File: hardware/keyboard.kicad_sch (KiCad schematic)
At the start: 10 parts, among them SW11 SW_Push, SW12 SW_Push, SW13 SW_Push, SW14 SW_Push, SW15 SW_Push, SW16 SW_Push, SW17 SW_Push, SW18 SW_Push, SW19 SW_Push

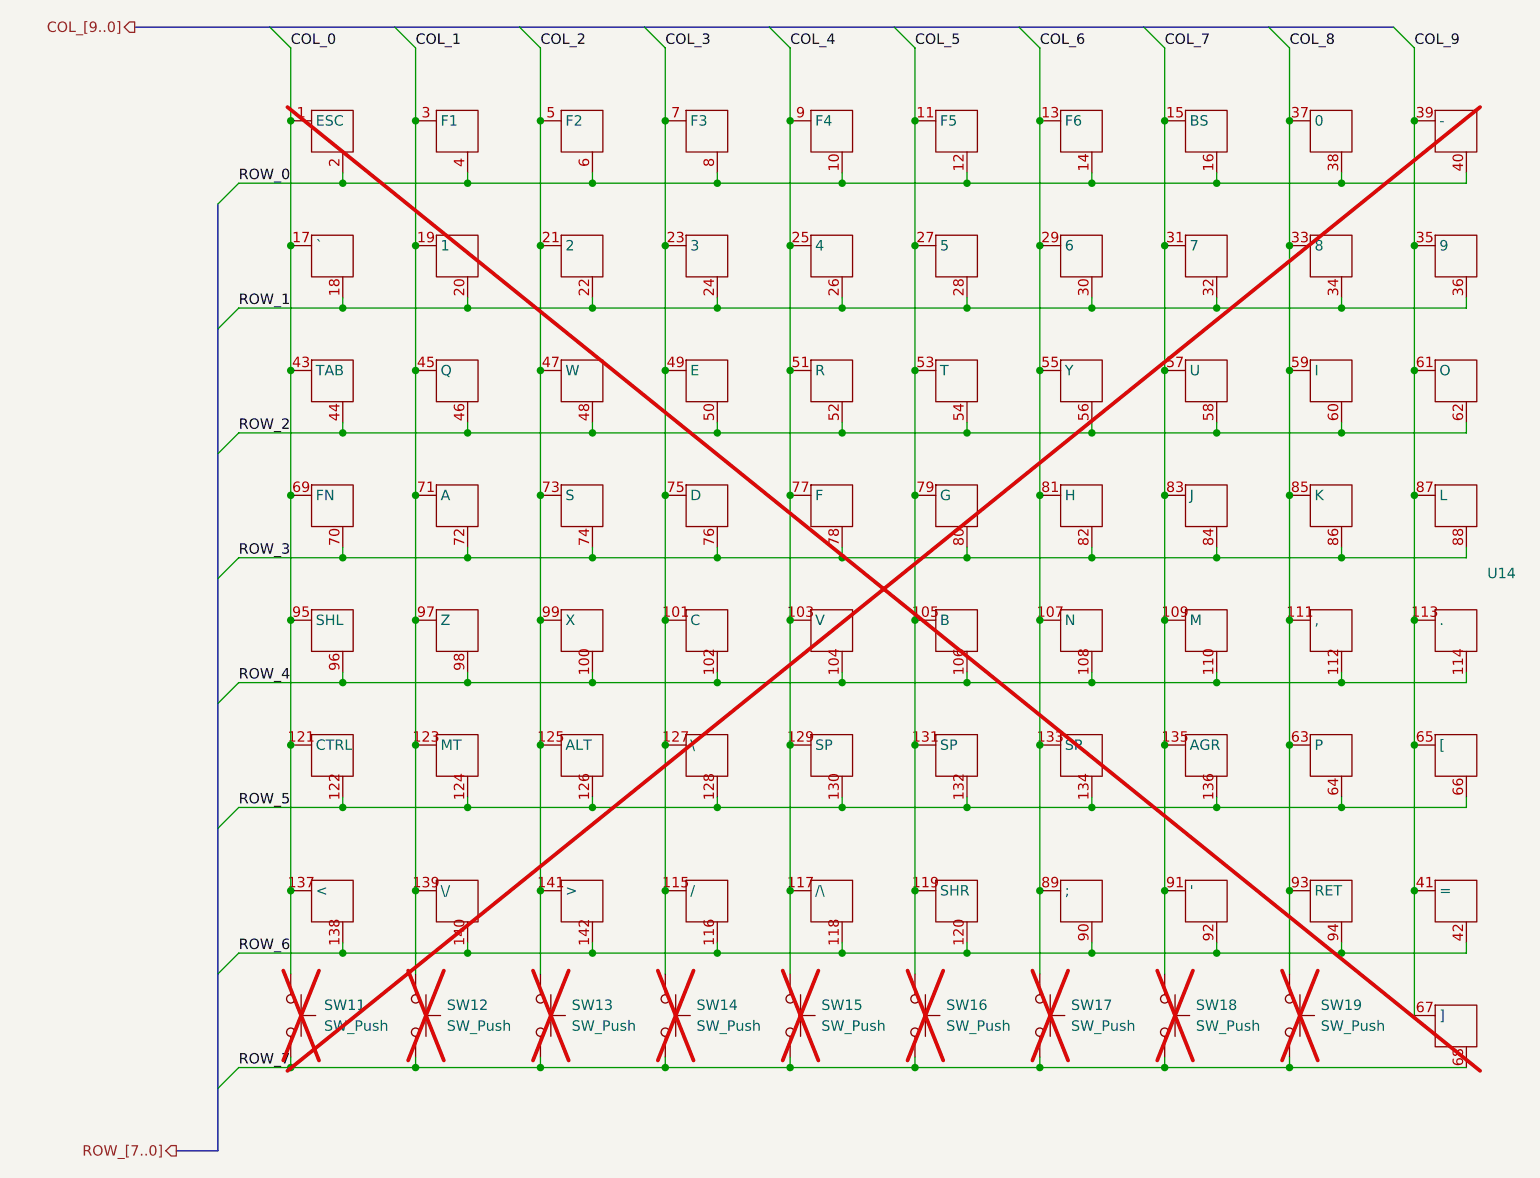
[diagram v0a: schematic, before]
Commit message: Removed old readme, added files.
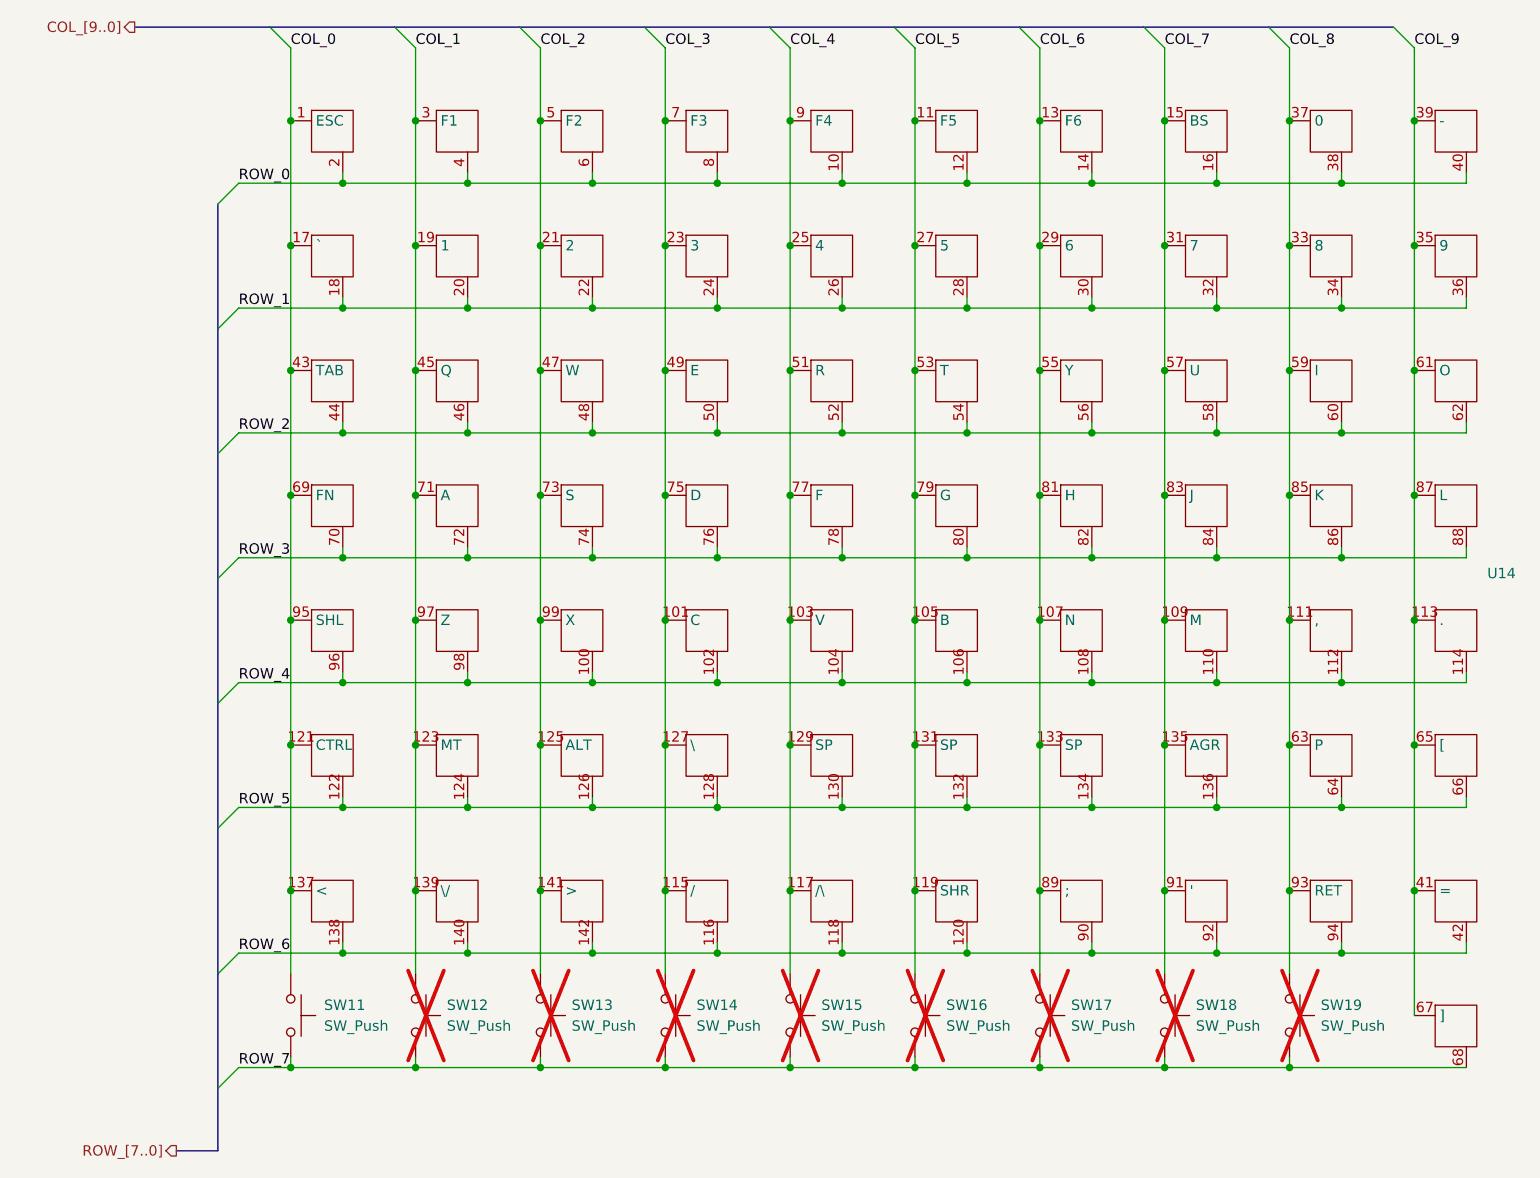
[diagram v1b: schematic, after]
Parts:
- SW11, U14: now fitted
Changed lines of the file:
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@@
+				)
+			)
+			(project "keyboard"
+				(path "/f3d86fab-5744-45a3-a365-b0c0c36d0bf2"
+					(reference "SW?")
+					(unit 1)
 				)
 			)
@@
 		(in_bom no)
 		(on_board yes)
-		(dnp yes)
+		(dnp no)
 		(property "Reference" "U14"
 			(at 229.87 93.3449 0)
@@
 				(path "/d0a98fce-b133-4503-8f8a-83b2a1eed591/83b47a1d-beff-4fad-8dc4-09477bd5c4c9"
 					(reference "U14")
+					(unit 1)
+				)
+			)
+			(project "keyboard"
+				(path "/f3d86fab-5744-45a3-a365-b0c0c36d0bf2"
+					(reference "U?")
 					(unit 1)
 				)
@@
 				)
 			)
+			(project "keyboard"
+				(path "/f3d86fab-5744-45a3-a365-b0c0c36d0bf2"
+					(reference "SW?")
+					(unit 1)
+				)
+			)
 		)
 	)
@@
 		(in_bom no)
 		(on_board no)
-		(dnp yes)
+		(dnp no)
 		(property "Reference" "SW11"
 			(at 87.884 146.05 90)
@@
 				(path "/d0a98fce-b133-4503-8f8a-83b2a1eed591/83b47a1d-beff-4fad-8dc4-09477bd5c4c9"
 					(reference "SW11")
+					(unit 1)
+				)
+			)
+			(project "keyboard"
+				(path "/f3d86fab-5744-45a3-a365-b0c0c36d0bf2"
+					(reference "SW?")
 					(unit 1)
 				)
@@
 				)
 			)
+			(project "keyboard"
+				(path "/f3d86fab-5744-45a3-a365-b0c0c36d0bf2"
+					(reference "SW?")
+					(unit 1)
+				)
+			)
 		)
 	)
@@
 				)
 			)
+			(project "keyboard"
+				(path "/f3d86fab-5744-45a3-a365-b0c0c36d0bf2"
+					(reference "SW?")
+					(unit 1)
+				)
+			)
 		)
 	)
@@
 				)
 			)
+			(project "keyboard"
+				(path "/f3d86fab-5744-45a3-a365-b0c0c36d0bf2"
+					(reference "SW?")
+					(unit 1)
+				)
+			)
 		)
 	)
@@
 				)
 			)
+			(project "keyboard"
+				(path "/f3d86fab-5744-45a3-a365-b0c0c36d0bf2"
+					(reference "SW?")
+					(unit 1)
+				)
+			)
 		)
 	)
@@
 				)
 			)
+			(project "keyboard"
+				(path "/f3d86fab-5744-45a3-a365-b0c0c36d0bf2"
+					(reference "SW?")
+					(unit 1)
+				)
+			)
 		)
 	)
@@
 				)
 			)
+			(project "keyboard"
+				(path "/f3d86fab-5744-45a3-a365-b0c0c36d0bf2"
+					(reference "SW?")
+					(unit 1)
+				)
+			)
 		)
 	)
+	(sheet_instances
+		(path "/"
+			(page "1")
+		)
+	)
+	(embedded_fonts no)
 )
